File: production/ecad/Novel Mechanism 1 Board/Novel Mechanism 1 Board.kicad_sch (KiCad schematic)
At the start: 0 parts

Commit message: Novel Mech 1 Commit
updated schematic, added components to libraries
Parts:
- added C1, C3, C7: 4.7u, symbol Device:C
- added C2, C4, C8: 0.1u, symbol Device:C
- added C5, C6, C9: 470p, symbol Device:C
- added R1, R2, R3, R4, R5, R6, R7, R8, R9: 5k, symbol Device:R_US
- added R10, R11, R12: 10k, symbol Device:R_US
- added RV1: R_Potentiometer, symbol Device:R_Potentiometer
- added RV2: FSR_1, symbol Device:R_Potentiometer
- added RV3: FSR_2, symbol Device:R_Potentiometer
- added U1, U2, U3: ~, symbol NM2_8bit_ADC:NM2_8bit_ADC
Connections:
- new net: R11.1, RV2.3
- new net: R12.1, RV3.3
- new net: R10.1, RV1.3
- new net +5V: C1.1, C2.1, C3.1, C4.1, C7.1, C8.1, R1.1, R2.1, R3.1, R4.1, R5.1, R6.1, R7.1, R8.1, R9.1, RV1.1, RV2.1, RV3.1, U1.1 (VA), U2.1 (VA), U3.1 (VA)
- new net FSR_1: C6.1, RV2.2, U2.3 (Vin)
- new net FSR_2: C9.1, RV3.2, U3.3 (Vin)
- new net GND: C1.2, C2.2, C3.2, C4.2, C5.2, C6.2, C7.2, C8.2, C9.2, R10.2, R11.2, R12.2, U1.2 (GND), U2.2 (GND), U3.2 (GND)
- new net I2C_SCL: R2.2, R5.2, R8.2, U1.5 (SCL), U2.5 (SCL), U3.5 (SCL)
- new net I2C_SDA: R1.2, R4.2, R7.2, U1.6 (SDA), U2.6 (SDA), U3.6 (SDA)
- new net INTERRUPT: R3.2, R6.2, R9.2, U1.4 (ADDR), U2.4 (ADDR), U3.4 (ADDR)
- new net LIN_POT: C5.1, RV1.2, U1.3 (Vin)

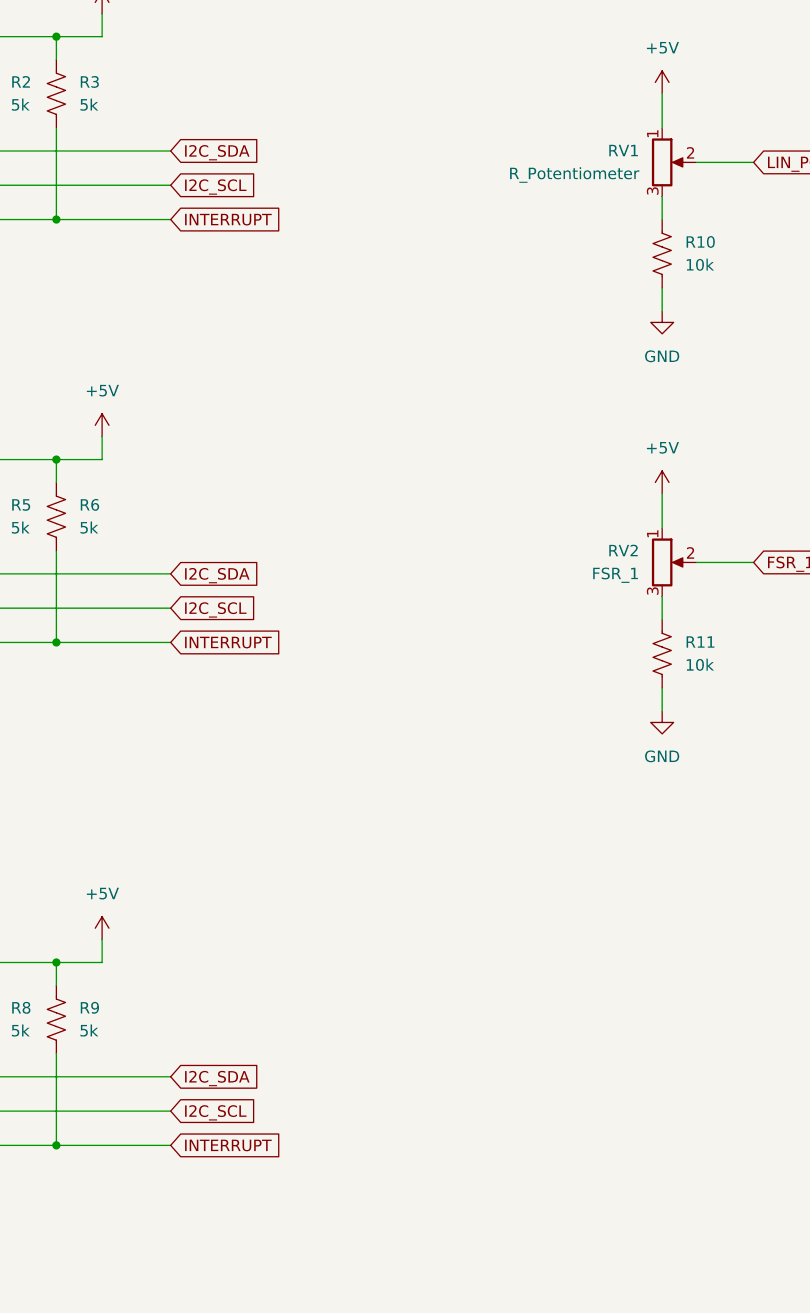
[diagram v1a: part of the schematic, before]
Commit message: Footprints
updated footprints and datasheets
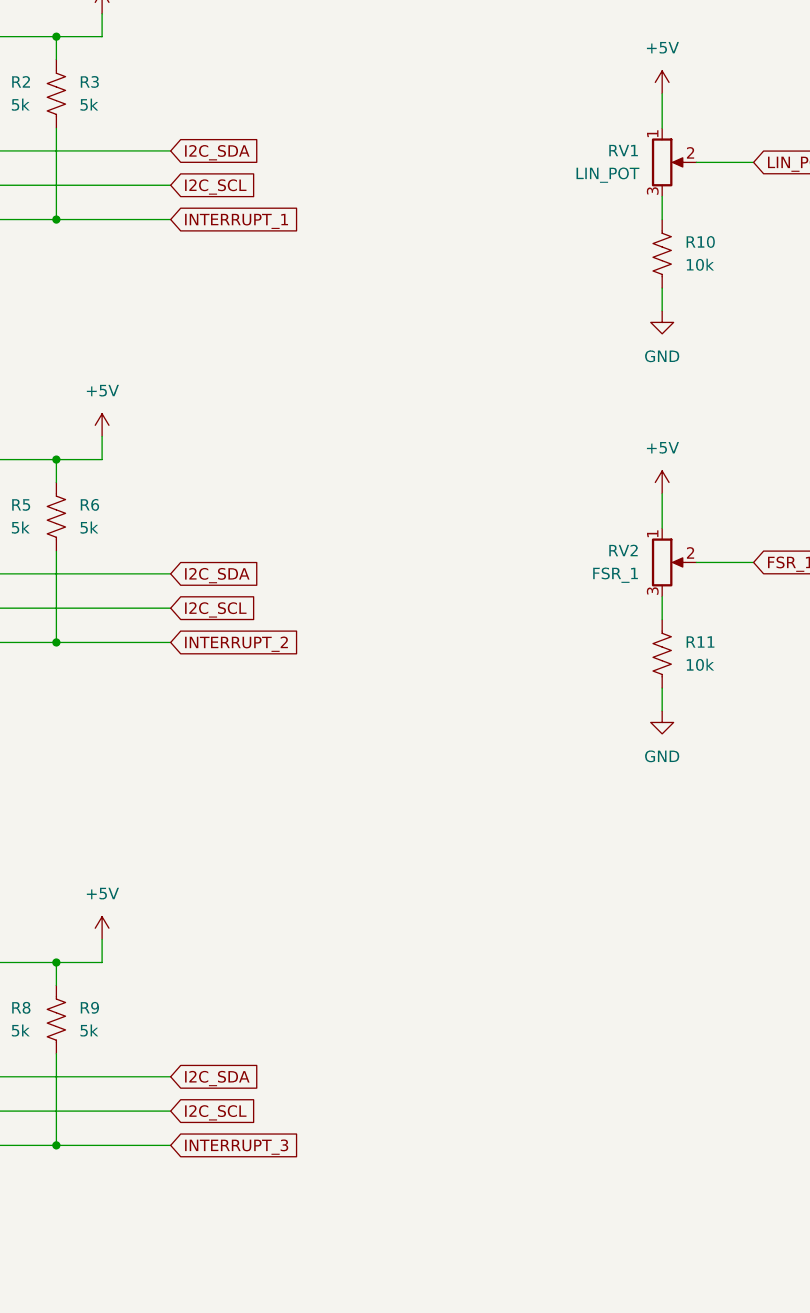
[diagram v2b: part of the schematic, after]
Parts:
- RV1: value R_Potentiometer -> LIN_POT
- U1, U2, U3: footprint (none) -> Sensify:NM1_8bit_ADC
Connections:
- removed net INTERRUPT: R3.2, R6.2, R9.2, U1.4 (ADDR), U2.4 (ADDR), U3.4 (ADDR)
- new net INTERRUPT_1: R3.2, U1.4 (ADDR)
- new net INTERRUPT_2: R6.2, U2.4 (ADDR)
- new net INTERRUPT_3: R9.2, U3.4 (ADDR)
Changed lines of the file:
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@@
     )
   )
-  (global_label "INTERRUPT" (shape input) (at 127 45.72 0) (fields_autoplaced)
+  (global_label "INTERRUPT_1" (shape input) (at 127 45.72 0) (fields_autoplaced)
     (effects (font (size 1.27 1.27)) (justify left))
-    (property "Intersheetrefs" "${INTERSHEET_REFS}" (at 140.1452 45.72 0)
+    (property "Intersheetrefs" "${INTERSHEET_REFS}" (at 142.3223 45.72 0)
       (effects (font (size 1.27 1.27)) (justify left) hide)
     )
@@
     )
   )
-  (global_label "INTERRUPT" (shape input) (at 127 148.59 0) (fields_autoplaced)
+  (global_label "INTERRUPT_3" (shape input) (at 127 148.59 0) (fields_autoplaced)
     (effects (font (size 1.27 1.27)) (justify left))
-    (property "Intersheetrefs" "${INTERSHEET_REFS}" (at 140.1452 148.59 0)
+    (property "Intersheetrefs" "${INTERSHEET_REFS}" (at 142.3223 148.59 0)
       (effects (font (size 1.27 1.27)) (justify left) hide)
     )
   )
-  (global_label "INTERRUPT" (shape input) (at 127 92.71 0) (fields_autoplaced)
+  (global_label "INTERRUPT_2" (shape input) (at 127 92.71 0) (fields_autoplaced)
     (effects (font (size 1.27 1.27)) (justify left))
-    (property "Intersheetrefs" "${INTERSHEET_REFS}" (at 140.1452 92.71 0)
+    (property "Intersheetrefs" "${INTERSHEET_REFS}" (at 142.3223 92.71 0)
       (effects (font (size 1.27 1.27)) (justify left) hide)
     )
@@
       (effects (font (size 1.27 1.27)))
     )
-    (property "Footprint" "" (at 86.36 88.9 0)
-      (effects (font (size 1.27 1.27)) hide)
-    )
-    (property "Datasheet" "" (at 86.36 88.9 0)
+    (property "Footprint" "Sensify:NM1_8bit_ADC" (at 86.36 88.9 0)
+      (effects (font (size 1.27 1.27)) hide)
+    )
+    (property "Datasheet" "https://www.ti.com/lit/ds/symlink/adc081c021.pdf?HQS=dis-dk-null-digikeymode-dsf-pf-null-wwe&ts=1728430135448&ref_url=https%253A%252F%252Fwww.ti.com%252Fgeneral%252Fdocs%252Fsuppproductinfo.tsp%253FdistId%253D10%2526gotoUrl%253Dhttps%253A%252F%252Fwww.ti.com%252Flit%252Fgpn%252Fadc081c021" (at 86.36 88.9 0)
       (effects (font (size 1.27 1.27)) hide)
     )
@@
       (effects (font (size 1.27 1.27)) hide)
     )
-    (property "Datasheet" "~" (at 181.61 83.82 0)
+    (property "Datasheet" "https://cdn2.hubspot.net/hubfs/3899023/Interlinkelectronics%20November2017/Docs/Datasheet_FSR.pdf" (at 181.61 83.82 0)
       (effects (font (size 1.27 1.27)) hide)
     )
@@
       (effects (font (size 1.27 1.27)))
     )
-    (property "Footprint" "" (at 86.36 41.91 0)
-      (effects (font (size 1.27 1.27)) hide)
-    )
-    (property "Datasheet" "" (at 86.36 41.91 0)
+    (property "Footprint" "Sensify:NM1_8bit_ADC" (at 86.36 41.91 0)
+      (effects (font (size 1.27 1.27)) hide)
+    )
+    (property "Datasheet" "https://www.ti.com/lit/ds/symlink/adc081c021.pdf?HQS=dis-dk-null-digikeymode-dsf-pf-null-wwe&ts=1728430135448&ref_url=https%253A%252F%252Fwww.ti.com%252Fgeneral%252Fdocs%252Fsuppproductinfo.tsp%253FdistId%253D10%2526gotoUrl%253Dhttps%253A%252F%252Fwww.ti.com%252Flit%252Fgpn%252Fadc081c021" (at 86.36 41.91 0)
       (effects (font (size 1.27 1.27)) hide)
     )
@@
       (effects (font (size 1.27 1.27)))
     )
-    (property "Footprint" "" (at 86.36 144.78 0)
-      (effects (font (size 1.27 1.27)) hide)
-    )
-    (property "Datasheet" "" (at 86.36 144.78 0)
+    (property "Footprint" "Sensify:NM1_8bit_ADC" (at 86.36 144.78 0)
+      (effects (font (size 1.27 1.27)) hide)
+    )
+    (property "Datasheet" "https://www.ti.com/lit/ds/symlink/adc081c021.pdf?HQS=dis-dk-null-digikeymode-dsf-pf-null-wwe&ts=1728430135448&ref_url=https%253A%252F%252Fwww.ti.com%252Fgeneral%252Fdocs%252Fsuppproductinfo.tsp%253FdistId%253D10%2526gotoUrl%253Dhttps%253A%252F%252Fwww.ti.com%252Flit%252Fgpn%252Fadc081c021" (at 86.36 144.78 0)
       (effects (font (size 1.27 1.27)) hide)
     )
@@
       (effects (font (size 1.27 1.27)) hide)
     )
-    (property "Datasheet" "~" (at 227.33 83.82 0)
+    (property "Datasheet" "https://cdn2.hubspot.net/hubfs/3899023/Interlinkelectronics%20November2017/Docs/Datasheet_FSR.pdf" (at 227.33 83.82 0)
       (effects (font (size 1.27 1.27)) hide)
     )
@@
       (effects (font (size 1.27 1.27)) (justify right))
     )
-    (property "Value" "R_Potentiometer" (at 179.07 40.64 0)
+    (property "Value" "LIN_POT" (at 179.07 40.64 0)
       (effects (font (size 1.27 1.27)) (justify right))
     )

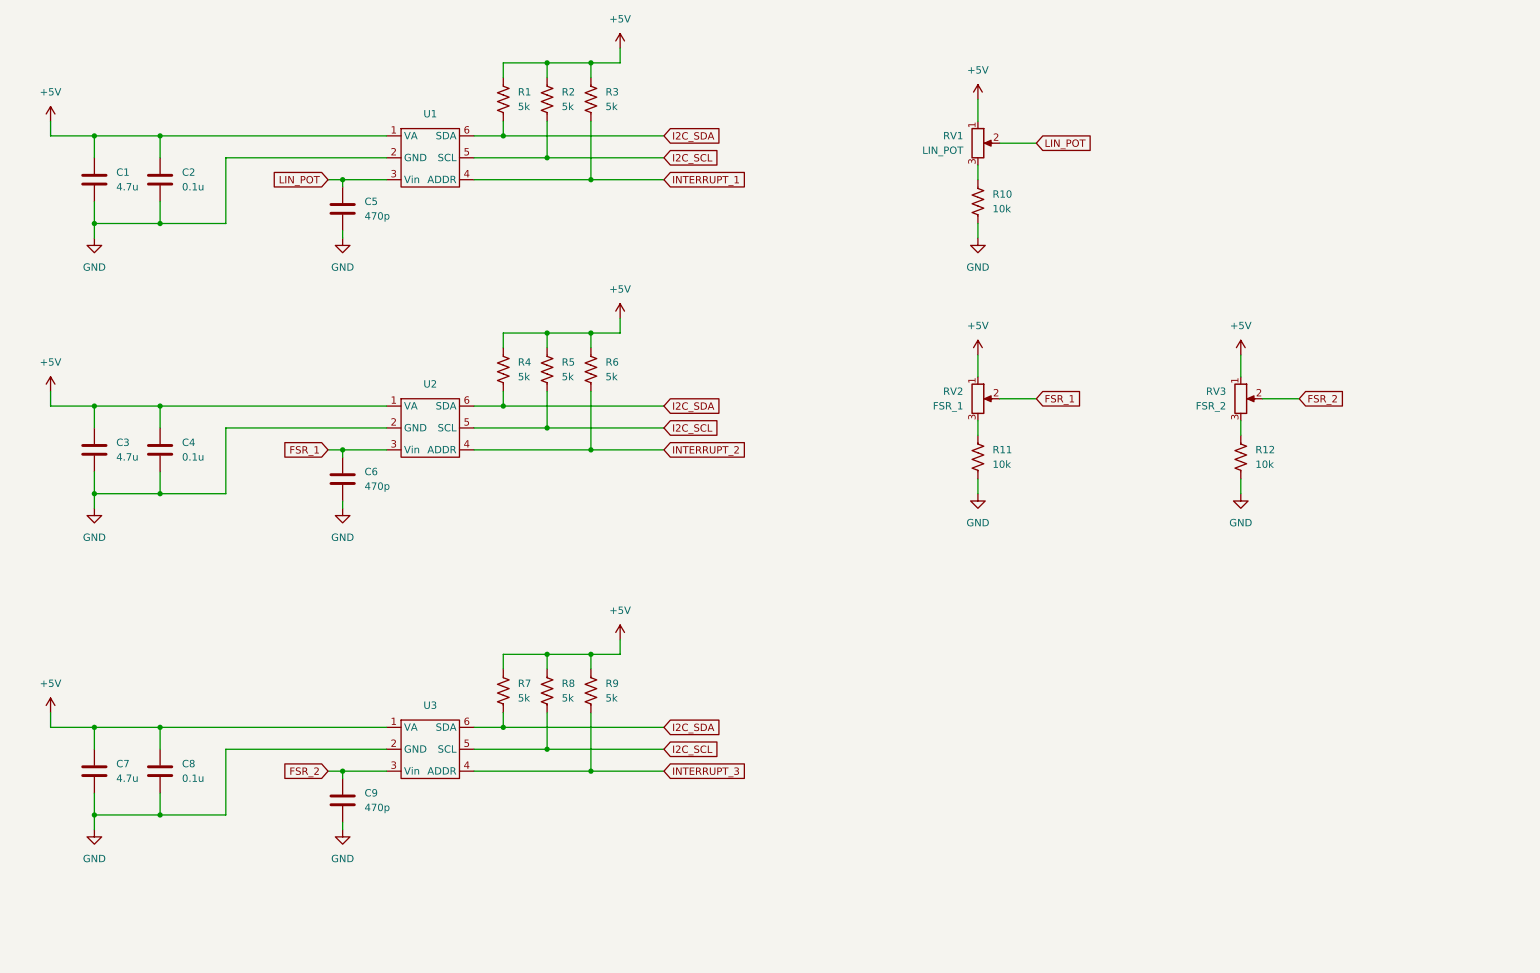
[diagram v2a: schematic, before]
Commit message: Changed ADC
converted ADC to 8 pin ADC, need to check footprint and add connector
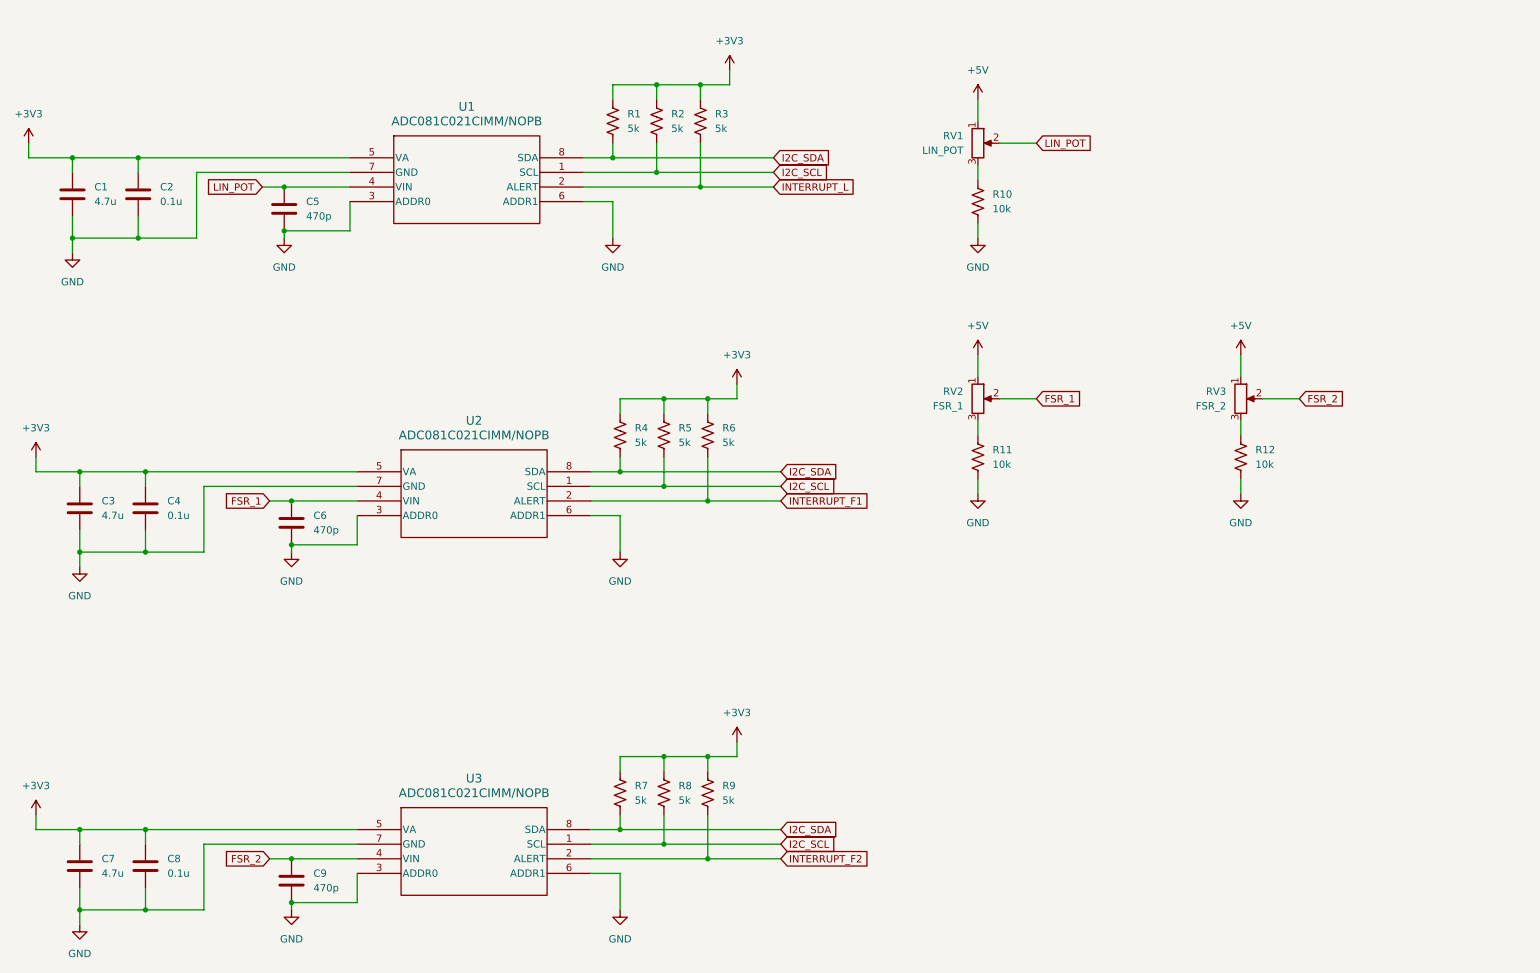
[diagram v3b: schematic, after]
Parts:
- removed U1, U2, U3: ~, Sensify:NM1_8bit_ADC, symbol NM2_8bit_ADC:NM2_8bit_ADC
- added U1, U2, U3: ADC081C021CIMM/NOPB, Package_TO_SOT_SMD:SOT-23-8, symbol ViseADC:ADC081C021CIMM_NOPB
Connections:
- net +5V: no longer C1.1, C2.1, C3.1, C4.1, C7.1, C8.1, R1.1, R2.1, R3.1, R4.1, R5.1, R6.1, R7.1, R8.1, R9.1
- net FSR_1: now also U2.4 (VIN)
- net FSR_2: now also U3.4 (VIN)
- net GND: now also U1.3 (ADDR0), U1.6 (ADDR1), U1.7 (GND), U2.3 (ADDR0), U2.6 (ADDR1), U2.7 (GND), U3.3 (ADDR0), U3.6 (ADDR1), U3.7 (GND)
- net I2C_SCL: now also U1.1 (SCL), U2.1 (SCL), U3.1 (SCL)
- net I2C_SDA: now also U1.8 (SDA), U2.8 (SDA), U3.8 (SDA)
- net LIN_POT: now also U1.4 (VIN)
- net INTERRUPT_1 renamed INTERRUPT_L
- net INTERRUPT_L: now also U1.2 (ALERT)
- net INTERRUPT_2 renamed INTERRUPT_F1
- net INTERRUPT_F1: now also U2.2 (ALERT)
- net INTERRUPT_3 renamed INTERRUPT_F2
- net INTERRUPT_F2: now also U3.2 (ALERT)
- new net +3V3: C1.1, C2.1, C3.1, C4.1, C7.1, C8.1, R1.1, R2.1, R3.1, R4.1, R5.1, R6.1, R7.1, R8.1, R9.1, U1.5 (VA), U2.5 (VA), U3.5 (VA)

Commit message: changed addresses
changed addresses
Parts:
- added R13, R14, R15, R16, R17, R18: 0, symbol Device:R_US
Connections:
- net +3V3: now also R15.2
- net GND: now also R13.2, R14.1, R16.1, R18.2; no longer U1.3 (ADDR0), U1.6 (ADDR1), U2.3 (ADDR0), U2.6 (ADDR1), U3.3 (ADDR0), U3.6 (ADDR1)
- new net: R18.1, U3.6 (ADDR1)
- new net: R14.2, U1.3 (ADDR0)
- new net: R13.1, U1.6 (ADDR1)
- new net: R16.2, U2.3 (ADDR0)
- new net: R15.1, U2.6 (ADDR1)
- new net: R17.2, U3.3 (ADDR0)
- new net +3.3V: R17.1
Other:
- note added: "ADDR:00"
- note added: "ADDR:01"
- note added: "ADDR:10"

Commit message: added connector
added connector
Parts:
- added J1, J2: ~, symbol ViseADC:6PIN_CONN
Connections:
- net +5V is gone; now on net +3V3: RV1.1, RV2.1, RV3.1
- net +3.3V: now also J2.6
- net GND: now also J2.4
- net INTERRUPT_F1: now also J1.4
- net INTERRUPT_F2: now also J1.5
- net I2C_SCL renamed SCL
- net SCL: now also J2.2
- net I2C_SDA renamed SDA
- net SDA: now also J2.3
- net INTERRUPT_L renamed INTERRUPT_LP
- net INTERRUPT_LP: now also J1.3
- new net DET: J2.5
- no-connect marks 0 -> 4
